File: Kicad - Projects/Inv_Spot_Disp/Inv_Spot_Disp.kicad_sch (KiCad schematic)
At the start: 43 parts, among them J1 PWM_Out, J2 Power_Supply, J3 Current_Sense, J4 Prog, J6 Temp_Sense, SW1 1, SW2 2, SW3 3, SW4 4, SW5 SW_Push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

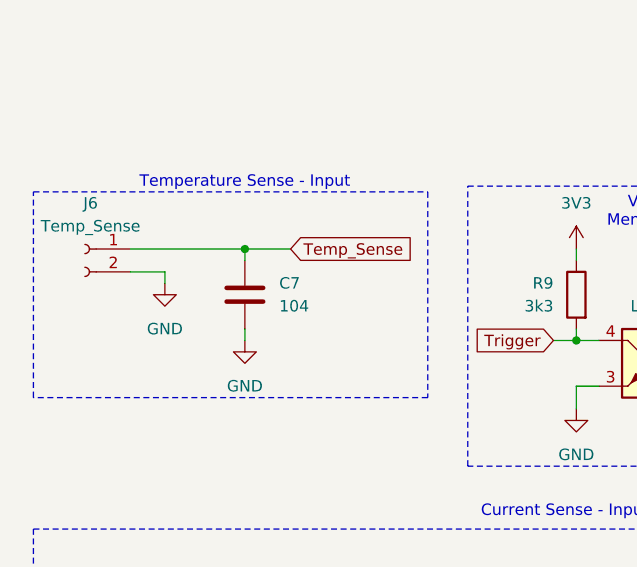
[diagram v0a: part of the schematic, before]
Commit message: Ajustes Finais
Ajustes finais de footprints e layouts
Considerando aumentar isolamento da trilha T- do IGBT Q2
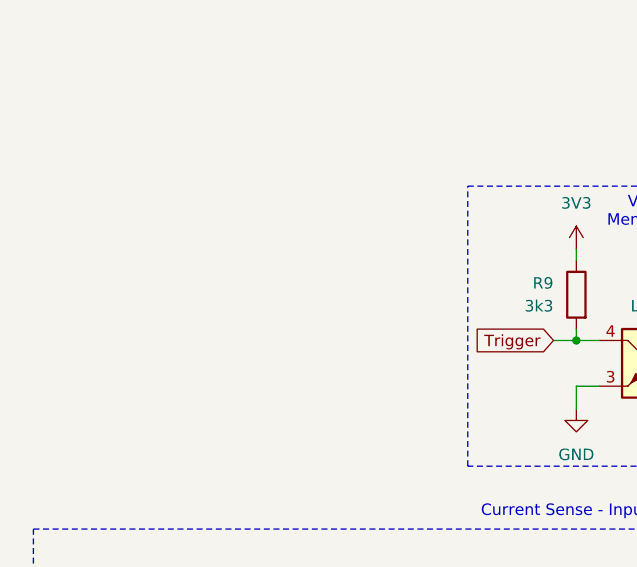
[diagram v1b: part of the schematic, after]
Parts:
- removed C7: 104, Capacitor_SMD:C_1206_3216Metric_Pad1.33x1.80mm_HandSolder, symbol Device:C
- removed J6: Temp_Sense, Connector_PinHeader_2.00mm:PinHeader_1x02_P2.00mm_Vertical, symbol Connector:Conn_01x02_Socket
- J1: footprint Connector_PinHeader_2.00mm:PinHeader_1x02_P2.00mm_Vertical -> Connector_PinHeader_2.54mm:PinHeader_1x02_P2.54mm_Vertical
- J2: footprint Connector_PinHeader_2.00mm:PinHeader_1x03_P2.00mm_Vertical -> Connector_PinHeader_2.54mm:PinHeader_1x03_P2.54mm_Vertical
- J4: footprint Connector_PinHeader_2.00mm:PinHeader_1x04_P2.00mm_Vertical -> Connector_PinHeader_2.54mm:PinHeader_1x04_P2.54mm_Vertical
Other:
- note removed: "Temperature Sense - Input"

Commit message: Ajustes Finais
Ajustes Finais do código, esquemáticos e layouts

Ainda faltam ajustes finos
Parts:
- added R13: 100, Resistor_SMD:R_1206_3216Metric_Pad1.30x1.75mm_HandSolder, symbol Device:R
- R6: value 56 -> 100
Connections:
- net GND: now also R13.2
- net at J3.1 (Pin_1), R6.1, U5.3 (+): now also R13.1
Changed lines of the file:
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@@
 	)
 	(junction
+		(at 41.91 152.4)
+		(diameter 0)
+		(color 0 0 0 0)
+	)
+	(junction
 		(at 77.47 110.49)
 		(diameter 0)
@@
 	(wire
 		(pts
+			(xy 41.91 152.4) (xy 44.45 152.4)
+		)
+		(stroke
+			(width 0)
+			(type default)
+		)
+	)
+	(wire
+		(pts
 			(xy 73.66 149.86) (xy 73.66 152.4)
 		)
@@
 	(wire
 		(pts
+			(xy 41.91 161.29) (xy 41.91 162.56)
+		)
+		(stroke
+			(width 0)
+			(type default)
+		)
+	)
+	(wire
+		(pts
 			(xy 194.31 102.87) (xy 194.31 101.6)
 		)
@@
 	(wire
 		(pts
+			(xy 41.91 152.4) (xy 41.91 153.67)
+		)
+		(stroke
+			(width 0)
+			(type default)
+		)
+	)
+	(wire
+		(pts
 			(xy 130.81 30.48) (xy 130.81 29.21)
 		)
@@
 	(wire
 		(pts
+			(xy 41.91 162.56) (xy 38.1 162.56)
+		)
+		(stroke
+			(width 0)
+			(type default)
+		)
+	)
+	(wire
+		(pts
 			(xy 120.65 172.72) (xy 120.65 173.99)
 		)
@@
 	(wire
 		(pts
-			(xy 38.1 152.4) (xy 44.45 152.4)
+			(xy 38.1 152.4) (xy 41.91 152.4)
 		)
 		(stroke
@@
 			)
 		)
-		(property "Value" "56"
+		(property "Value" "100"
 			(at 35.56 158.7499 0)
 			(show_name no)
@@
 					(unit 1)
 				)
+			)
+		)
+	)
+	(symbol
+		(lib_id "Device:R")
+		(at 41.91 157.48 0)
+		(unit 1)
+		(body_style 1)
+		(exclude_from_sim no)
+		(in_bom yes)
+		(on_board yes)
+		(in_pos_files yes)
+		(dnp no)
+		(property "Reference" "R13"
+			(at 44.45 156.2099 0)
+			(show_name no)
+			(do_not_autoplace no)
+			(effects
+				(font
+					(size 1.27 1.27)
+				)
+				(justify left)
+			)
+		)
+		(property "Value" "100"
+			(at 44.45 158.7499 0)
+			(show_name no)
+			(do_not_autoplace no)
+			(effects
+				(font
+					(size 1.27 1.27)
+				)
+				(justify left)
+			)
+		)
+		(property "Footprint" "Resistor_SMD:R_1206_3216Metric_Pad1.30x1.75mm_HandSolder"
+			(at 40.132 157.48 90)
+			(hide yes)
+			(show_name no)
+			(do_not_autoplace no)
+			(effects
+				(font
+					(size 1.27 1.27)
+				)
+			)
+		)
+		(property "Datasheet" ""
+			(at 41.91 157.48 0)
+			(hide yes)
+			(show_name no)
+			(do_not_autoplace no)
+			(effects
+				(font
+					(size 1.27 1.27)
+				)
+			)
+		)
+		(property "Description" "Resistor"
+			(at 41.91 157.48 0)
+			(hide yes)
+			(show_name no)
+			(do_not_autoplace no)
+			(effects
+				(font
+					(size 1.27 1.27)
+				)
+			)
+		)
+		(pin "2"
+		)
+		(pin "1"
+		)
+		(instances
+			(project "Inv_Spot_Disp"
+				(path "/016976b8-e488-405d-b5a2-1b3e7431e7ce"
+					(reference "R13")
+					(unit 1)
+				)

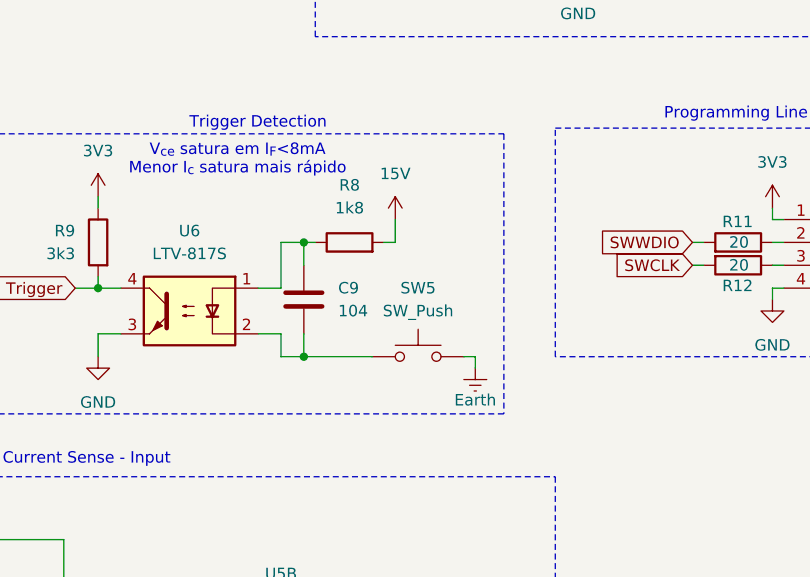
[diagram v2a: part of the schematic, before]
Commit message: Ajustes de Isolamento e Espaçamento
Ajustes no isolamento de trilhas de alta tensão na placa de potência e no espaçamento dos capacitores dos IGBTs

Ajustes nas posições de componentes na placa de display

Ajustado ADC para aumentar período de amostragem
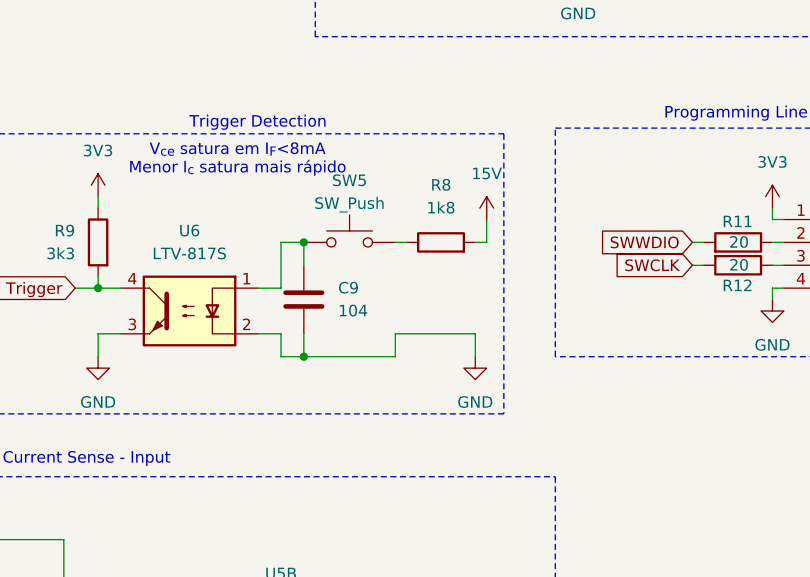
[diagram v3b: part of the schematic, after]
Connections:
- net GND: now also C9.2, U6.2
- net at C9.1, U6.1: now also SW5.1; no longer R8.1
- net Earth: no longer names the net of SW5.2
- net Earth: now also R8.1
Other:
- moved on the sheet: R8, SW5
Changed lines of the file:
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@@
 	)
 	(junction
+		(at 100.33 118.11)
+		(diameter 0)
+		(color 0 0 0 0)
+	)
+	(junction
 		(at 73.66 39.37)
 		(diameter 0)
@@
 	)
 	(junction
-		(at 41.91 152.4)
-		(diameter 0)
-		(color 0 0 0 0)
-	)
-	(junction
-		(at 77.47 110.49)
+		(at 100.33 105.41)
 		(diameter 0)
 		(color 0 0 0 0)
 	)
 	(junction
-		(at 46.99 168.91)
+		(at 41.91 152.4)
 		(diameter 0)
 		(color 0 0 0 0)
 	)
 	(junction
-		(at 100.33 105.41)
+		(at 77.47 110.49)
 		(diameter 0)
 		(color 0 0 0 0)
 	)
 	(junction
-		(at 100.33 118.11)
+		(at 46.99 168.91)
 		(diameter 0)
 		(color 0 0 0 0)
@@
 	(wire
 		(pts
-			(xy 110.49 105.41) (xy 110.49 102.87)
+			(xy 120.65 102.87) (xy 120.65 105.41)
 		)
 		(stroke
@@
 	(wire
 		(pts
-			(xy 119.38 118.11) (xy 119.38 119.38)
-		)
-		(stroke
-			(width 0)
-			(type default)
-		)
-	)
-	(wire
-		(pts
 			(xy 201.93 39.37) (xy 199.39 39.37)
 		)
@@
 	(wire
 		(pts
-			(xy 118.11 118.11) (xy 119.38 118.11)
+			(xy 143.51 105.41) (xy 144.78 105.41)
 		)
 		(stroke
@@
 	(wire
 		(pts
-			(xy 143.51 105.41) (xy 144.78 105.41)
+			(xy 73.66 49.53) (xy 73.66 50.8)
 		)
 		(stroke
@@
 	(wire
 		(pts
-			(xy 73.66 49.53) (xy 73.66 50.8)
+			(xy 119.38 118.11) (xy 119.38 115.57)
 		)
 		(stroke
@@
 	(wire
 		(pts
+			(xy 119.38 105.41) (xy 120.65 105.41)
+		)
+		(stroke
+			(width 0)
+			(type default)
+		)
+	)
+	(wire
+		(pts
 			(xy 204.47 143.51) (xy 209.55 143.51)
 		)
@@
 	(wire
 		(pts
-			(xy 100.33 118.11) (xy 107.95 118.11)
-		)
-		(stroke
-			(width 0)
-			(type default)
-		)
-	)
-	(wire
-		(pts
 			(xy 46.99 39.37) (xy 38.1 39.37)
 		)
@@
 	(wire
 		(pts
-			(xy 146.05 60.96) (xy 143.51 60.96)
+			(xy 110.49 105.41) (xy 111.76 105.41)
 		)
 		(stroke
@@
 	(wire
 		(pts
-			(xy 115.57 163.83) (xy 115.57 162.56)
+			(xy 146.05 60.96) (xy 143.51 60.96)
 		)
 		(stroke
@@
 	(wire
 		(pts
-			(xy 38.1 153.67) (xy 38.1 152.4)
+			(xy 115.57 163.83) (xy 115.57 162.56)
 		)
 		(stroke
@@
 	(wire
 		(pts
-			(xy 243.84 152.4) (xy 243.84 153.67)
+			(xy 38.1 153.67) (xy 38.1 152.4)
 		)
 		(stroke
@@
 	(wire
 		(pts
-			(xy 184.15 152.4) (xy 184.15 153.67)
+			(xy 243.84 152.4) (xy 243.84 153.67)
 		)
 		(stroke
@@
 	(wire
 		(pts
-			(xy 109.22 105.41) (xy 110.49 105.41)
+			(xy 184.15 152.4) (xy 184.15 153.67)
 		)
 		(stroke
@@
 	(wire
 		(pts
+			(xy 100.33 118.11) (xy 110.49 118.11)
+		)
+		(stroke
+			(width 0)
+			(type default)
+		)
+	)
+	(wire
+		(pts
 			(xy 273.05 105.41) (xy 273.05 109.22)
 		)
@@
 	(wire
 		(pts
-			(xy 100.33 105.41) (xy 101.6 105.41)
+			(xy 29.21 63.5) (xy 29.21 62.23)
 		)
 		(stroke
@@
 	(wire
 		(pts
-			(xy 29.21 63.5) (xy 29.21 62.23)
+			(xy 119.38 115.57) (xy 110.49 115.57)
 		)
 		(stroke
@@
 	(wire
 		(pts
+			(xy 110.49 115.57) (xy 110.49 118.11)
+		)
+		(stroke
+			(width 0)
+			(type default)
+		)
+	)
+	(wire
+		(pts
 			(xy 73.66 162.56) (xy 69.85 162.56)
 		)
@@
 	(symbol
 		(lib_id "Device:R")
-		(at 105.41 105.41 90)
+		(at 115.57 105.41 90)
 		(unit 1)
 		(body_style 1)
@@
 		(fields_autoplaced yes)
 		(property "Reference" "R8"
-			(at 105.41 99.06 90)
+			(at 115.57 99.06 90)
 			(show_name no)
 			(do_not_autoplace no)
@@
 		)
 		(property "Value" "1k8"
-			(at 105.41 101.6 90)
+			(at 115.57 101.6 90)
 			(show_name no)
 			(do_not_autoplace no)
@@
 		)
 		(property "Footprint" "Resistor_SMD:R_1206_3216Metric_Pad1.30x1.75mm_HandSolder"
-			(at 105.41 107.188 90)
+			(at 115.57 107.188 90)
 			(hide yes)
 			(show_name no)
@@
 		)
 		(property "Datasheet" ""
-			(at 105.41 105.41 0)
+			(at 115.57 105.41 0)
 			(hide yes)
 			(show_name no)
@@
 		)
 		(property "Description" "Resistor"
-			(at 105.41 105.41 0)
+			(at 115.57 105.41 0)
 			(hide yes)
 			(show_name no)
@@
 	)
 	(symbol
-		(lib_id "power:Earth")
-		(at 119.38 119.38 0)
-		(unit 1)
-		(body_style 1)
-		(exclude_from_sim no)
-		(in_bom yes)
-		(on_board yes)
-		(in_pos_files yes)
-		(dnp no)
-		(property "Reference" "#PWR011"
-			(at 119.38 125.73 0)
-			(hide yes)
-			(show_name no)
-			(do_not_autoplace no)
-			(effects
-				(font
-					(size 1.27 1.27)
-				)
-			)
-		)
-		(property "Value" "Earth"
-			(at 119.38 122.936 0)
-			(show_name no)
-			(do_not_autoplace no)
-			(effects
-				(font
-					(size 1.27 1.27)
-				)
-			)
-		)
-		(property "Footprint" ""
-			(at 119.38 119.38 0)
-			(hide yes)
-			(show_name no)
-			(do_not_autoplace no)
-			(effects
-				(font
-					(size 1.27 1.27)
-				)
-			)
-		)
-		(property "Datasheet" ""
-			(at 119.38 119.38 0)
-			(hide yes)
-			(show_name no)
-			(do_not_autoplace no)
-			(effects
-				(font
-					(size 1.27 1.27)
-				)
-			)
-		)
-		(property "Description" "Power symbol creates a global label with name \"Earth\""
-			(at 119.38 119.38 0)
-			(hide yes)
-			(show_name no)
-			(do_not_autoplace no)
-			(effects
-				(font
-					(size 1.27 1.27)
-				)
-			)
-		)
-		(pin "1"
-		)
-		(instances
-			(project "Inv_Spot_Disp"
-				(path "/016976b8-e488-405d-b5a2-1b3e7431e7ce"
-					(reference "#PWR011")
-					(unit 1)
-				)
-			)
-		)
-	)
-	(symbol
 		(lib_id "power:GND")
 		(at 120.65 173.99 0)
@@
 	)
 	(symbol
-		(lib_id "Switch:SW_Push")
-		(at 113.03 118.11 0)
+		(lib_id "power:GND")
+		(at 119.38 118.11 0)
 		(unit 1)
 		(body_style 1)
@@
 		(dnp no)
 		(fields_autoplaced yes)
+		(property "Reference" "#PWR024"
+			(at 119.38 124.46 0)
+			(hide yes)
+			(show_name no)
+			(do_not_autoplace no)
+			(effects
+				(font
+					(size 1.27 1.27)
+				)
+			)
+		)
+		(property "Value" "GND"
+			(at 119.38 123.19 0)
+			(show_name no)
+			(do_not_autoplace no)
+			(effects
+				(font
+					(size 1.27 1.27)
+				)
+			)
+		)
+		(property "Footprint" ""
+			(at 119.38 118.11 0)
+			(hide yes)
+			(show_name no)
+			(do_not_autoplace no)
+			(effects
+				(font
+					(size 1.27 1.27)
+				)
+			)
+		)
+		(property "Datasheet" ""
+			(at 119.38 118.11 0)
+			(hide yes)
+			(show_name no)
+			(do_not_autoplace no)
+			(effects
+				(font
+					(size 1.27 1.27)
+				)
+			)
+		)
+		(property "Description" "Power symbol creates a global label with name \"GND\" , ground"
+			(at 119.38 118.11 0)
+			(hide yes)
+			(show_name no)
+			(do_not_autoplace no)
+			(effects
+				(font
+					(size 1.27 1.27)
+				)
+			)
+		)
+		(pin "1"
+		)
+		(instances
+			(project "Inv_Spot_Disp"
+				(path "/016976b8-e488-405d-b5a2-1b3e7431e7ce"
+					(reference "#PWR024")
+					(unit 1)
+				)
+			)
+		)
+	)
+	(symbol
+		(lib_id "Switch:SW_Push")
+		(at 105.41 105.41 0)
+		(unit 1)
+		(body_style 1)
+		(exclude_from_sim no)
+		(in_bom yes)
+		(on_board yes)
+		(in_pos_files yes)
+		(dnp no)
 		(property "Reference" "SW5"
-			(at 113.03 110.49 0)
+			(at 105.41 98.552 0)
 			(show_name no)
 			(do_not_autoplace no)
@@
 		)
 		(property "Value" "SW_Push"
-			(at 113.03 113.03 0)
+			(at 105.41 101.092 0)
 			(show_name no)
 			(do_not_autoplace no)
@@
 		)
 		(property "Footprint" "Button_Switch_THT:SW_PUSH_1P1T_6x3.5mm_H4.3_APEM_MJTP1243"
-			(at 113.03 113.03 0)
+			(at 105.41 100.33 0)
 			(hide yes)
 			(show_name no)
@@
 		)
 		(property "Datasheet" ""
-			(at 113.03 113.03 0)
+			(at 105.41 100.33 0)
 			(hide yes)
 			(show_name no)
@@
 		)
 		(property "Description" "Push button switch, generic, two pins"
-			(at 113.03 118.11 0)
+			(at 105.41 105.41 0)
 			(hide yes)
 			(show_name no)
@@
 	(symbol
 		(lib_id "power:VCC")
-		(at 110.49 102.87 0)
+		(at 120.65 102.87 0)
 		(unit 1)
 		(body_style 1)
@@
 		(fields_autoplaced yes)
 		(property "Reference" "#PWR051"
-			(at 110.49 106.68 0)
+			(at 120.65 106.68 0)
 			(hide yes)
 			(show_name no)
@@
 		)
 		(property "Value" "15V"
-			(at 110.49 97.79 0)
+			(at 120.65 97.79 0)
 			(show_name no)
 			(do_not_autoplace no)
@@
 		)
 		(property "Footprint" ""
-			(at 110.49 102.87 0)
+			(at 120.65 102.87 0)
 			(hide yes)
 			(show_name no)
@@
 		)
 		(property "Datasheet" ""
-			(at 110.49 102.87 0)
+			(at 120.65 102.87 0)
 			(hide yes)
 			(show_name no)
@@
 		)
 		(property "Description" "Power symbol creates a global label with name \"VCC\""
-			(at 110.49 102.87 0)
+			(at 120.65 102.87 0)
 			(hide yes)
 			(show_name no)

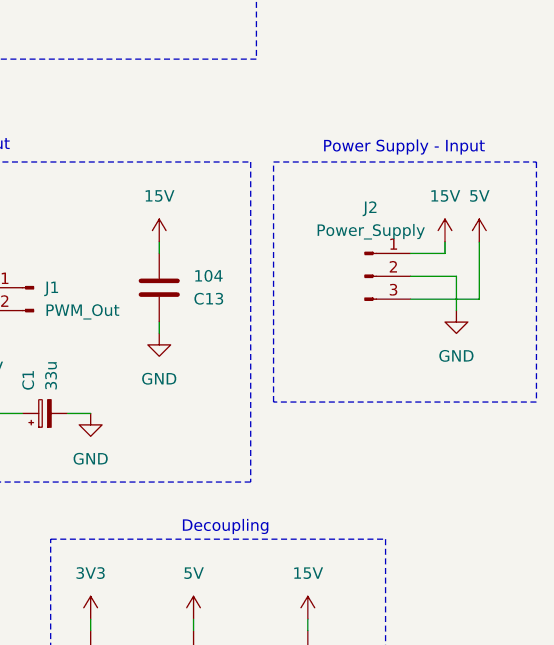
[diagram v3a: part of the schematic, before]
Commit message: Adicionado LED - Temperatura
Adicionado LED na linha de 15V que desliga quando proteção térmica é acionada

Adicionados PDFs para impressão
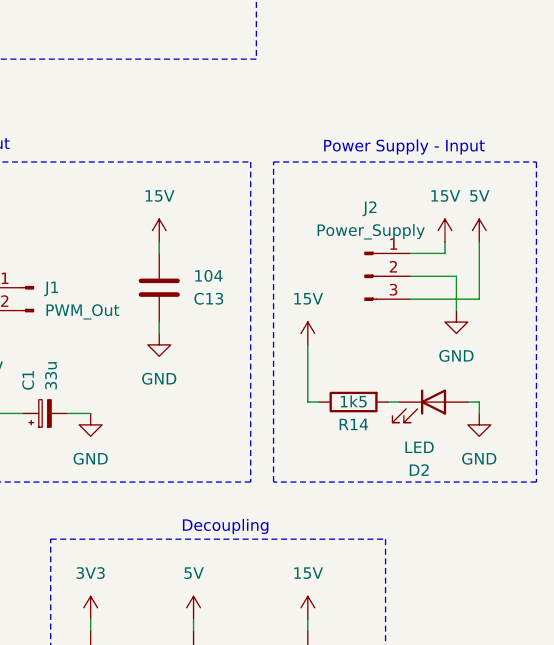
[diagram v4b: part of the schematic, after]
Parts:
- added D2: LED, LED_THT:LED_D5.0mm, symbol Device:LED
- added R14: 1k5, Resistor_SMD:R_1206_3216Metric_Pad1.30x1.75mm_HandSolder, symbol Device:R
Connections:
- net 15V: now also R14.1
- net GND: now also D2.2 (A)
- new net: D2.1 (K), R14.2
